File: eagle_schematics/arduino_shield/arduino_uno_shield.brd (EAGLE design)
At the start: 53 x 57.1 mm, 20 parts

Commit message: save
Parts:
- removed A1, A2, A3, A4, A5, A6, A7, A8: (no value), SparkFun-Connectors:1X03
- removed AUDIO_JACK: (no value), SparkFun-Connectors:AUDIO-JACK
- removed FRAME3: FRAME-LETTER, SparkFun-Aesthetics:CREATIVE_COMMONS
- removed MCP3208: MCP3208-CI/P, Microchip_By_element14_Batch_1:DIP254P762X432-16
- removed MCP4921: MCP4921-E/P, Microchip_By_element14_Batch_1:DIP254P762X432-8
- added ADC1_MIC: (no value), SparkFun-Connectors:1X03_LOCK
- added ADC2, ADC3, ADC4: TRIMPOT-PTH-KNOB, SparkFun-Electromechanical:3386U
- added JP1: (no value), SparkFun-Connectors:AUDIO-JACK
- added R4: (no value), SparkFun-Resistors:AXIAL-0.3
- added U$2: MCP3204-CI/P, Microchip_By_element14_Batch_1:DIP254P762X432-14
- added U1: ARDUINO_R3_SHIELD, SparkFun-Boards:UNO_R3_SHIELD
- C1: device SparkFun-Passives:CAP-PTH-SMALL -> SparkFun-Capacitors:CAP-PTH-5MM
- C2: device SparkFun-Passives:CPOL-RADIAL-10UF-25V -> SparkFun-Capacitors:CPOL-RADIAL-10UF-25V
- EXT_LED: value M023.5MM -> M02LOCK; device SparkFun-Connectors:SCREWTERMINAL-3.5MM-2 -> SparkFun-Connectors:1X02_LOCK
- R1: value 1.5K -> 330; device SparkFun-Passives:AXIAL-0.4 -> SparkFun-Resistors:AXIAL-0.3
- R2: value 1K -> 1.5k; device SparkFun-Passives:AXIAL-0.4 -> SparkFun-Resistors:AXIAL-0.3
- R3: value 330 -> 1k; device SparkFun-Passives:AXIAL-0.4 -> SparkFun-Resistors:AXIAL-0.3
- U$1: value ARDUINO_R3_SHIELD -> MCP4921-E/P; device SparkFun-Boards:UNO_R3_SHIELD -> Microchip_By_element14_Batch_1:DIP254P762X432-8
- moved R3 53.6 mm to (26.7, 16.5), turned to 0 degrees
- moved C2 25.9 mm to (44.5, 16.5), turned to 0 degrees
- moved EXT_LED 20.4 mm to (30.5, 3.81)
- moved R2 20.4 mm to (26.7, 19.1)
- moved U$1 19.9 mm to (17.8, 11.4)
- moved C1 19.4 mm to (36.8, 15.2), turned to 0 degrees
- moved R1 16.6 mm to (14.0, 53.3)
- moved LED 15.3 mm to (15.2, 47.0), turned to 0 degrees
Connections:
- removed net AUD: A1.2, MCP3208.1
- removed net N$10: LED.A, R3.P$1
- removed net N$11: MCP4921.5, U$1.D8
- removed net N$12: EXT_LED.1, R3.P$2, U$1.D6
- removed net N$14: A3.2, MCP3208.3
- removed net N$15: A4.2, MCP3208.4
- removed net N$16: A6.2, MCP3208.6
- removed net N$17: A7.2, MCP3208.7
- removed net N$18: A8.2, MCP3208.8
- removed net N$8: C1.1, C2.1, R1.P$2
- removed net N$9: AUDIO_JACK.RING, AUDIO_JACK.TIP, C2.2, R2.P$2
- removed net SPI_CLK: MCP3208.13, MCP4921.3, U$1.D13
- removed net SPI_MISO: MCP3208.12, U$1.D12
- removed net SPI_MOSI: MCP3208.11, MCP4921.4, U$1.D11
- new net ADC1: ADC1_MIC.1, U$2.1
- new net ADC2: ADC2.2, U$2.2
- new net ADC3: ADC3.2, U$2.3
- new net ADC4: ADC4.2, U$2.4
- new net LDAC: U$1.5, U1.D8
- new net LED: R1.P$1, R4.P$1, U1.D6
- new net MISO: U$2.10, U1.D12
- new net MOSI: U$1.4, U$2.9, U1.D11
- new net N$4: C2.2, JP1.RING, JP1.TIP, R3.P$2
- new net N$5: EXT_LED.1, R4.P$2
- new net SCK: U$1.3, U$2.11, U1.D13
- net 3.3V: now also ADC1_MIC.3, ADC2.1, ADC3.1, ADC4.1, U$1.6, U$2.13, U1.3.3V; no longer A1.3, A2.3, A3.3, A4.3, A5.3, A6.3, A7.3, A8.3, MCP3208.15, MCP4921.6, U$1.3.3V
- net 5V: now also U$1.1, U$2.14, U1.5V; no longer MCP3208.16, MCP4921.1, U$1.5V
- net CS_ADC: now also U$2.8, U1.D10; no longer MCP3208.10, U$1.D10
- net CS_DAC: now also U$1.2, U1.D9; no longer MCP4921.2, U$1.D9
- net GND: now also ADC1_MIC.2, ADC2.3, ADC3.3, ADC4.3, JP1.SLEEVE, R3.P$1, U$1.7, U$2.12, U$2.7, U1.GND@0; no longer A1.1, A2.1, A3.1, A4.1, A5.1, A6.1, A7.1, A8.1, AUDIO_JACK.SLEEVE, MCP3208.14, MCP3208.9, MCP4921.7, R2.P$1, U$1.GND@0, U$1.GND@1, U$1.GND@2
- net N$1: now also LED.A, R1.P$2; no longer A5.2, MCP3208.5
- net N$2: now also R2.P$1, U$1.8; no longer A2.2, MCP3208.2
- net N$3: now also C1.1, C2.1, R2.P$2; no longer MCP4921.8, R1.P$1
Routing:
- net GND: track 204.1 -> 0.00 mm
- net 3.3V: track 97.2 -> 0.00 mm
- net N$12: track 62.3 -> 0.00 mm
- net 5V: track 50.5 -> 0.00 mm
- net N$1: track 36.8 -> 0.00 mm
- net AUD: track 35.7 -> 0.00 mm
- net N$16: track 34.9 -> 0.00 mm
- net N$11: track 33.5 -> 0.00 mm
- net CS_DAC: track 33.3 -> 0.00 mm
- net N$2: track 32.1 -> 0.00 mm
- net SPI_MOSI: track 32.0 -> 0.00 mm
- net N$9: track 29.3 -> 0.00 mm
- net N$17: track 28.3 -> 0.00 mm
- net N$18: track 23.9 -> 0.00 mm
- net SPI_CLK: track 23.7 -> 0.00 mm
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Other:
- board text removed: "3V"
- board text removed: "GND"
- board text removed: "IN"
- board text removed: "Ultimate Voice Changer Shield v1.0.1"
- board text removed: "theotherandygrove.com"

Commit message: save
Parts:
- moved EXT_LED 20.5 mm to (48.3, 14.0)
- moved C2 14.5 mm to (33.0, 7.62), turned to 90 degrees
- moved C1 13.3 mm to (24.1, 11.4), turned to 180 degrees
- moved R3 10.5 mm to (24.1, 6.35)
- moved R4 10.2 mm to (40.6, 14.0)
- moved ADC2 3.81 mm to (39.4, 22.9)
- moved R2 3.59 mm to (24.1, 16.5)
- moved LED 3.59 mm to (12.7, 44.5), turned to 90 degrees
- moved R1 2.84 mm to (12.7, 50.8)
- moved U$1 2.84 mm to (16.5, 8.89)
- moved U$2 2.84 mm to (8.89, 36.8)
- moved ADC3 2.54 mm to (39.4, 35.6)
- moved ADC1_MIC 1.80 mm to (22.9, 31.8)
- moved ADC4 1.27 mm to (39.4, 48.3)
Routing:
- net GND: track 0.00 -> 164.3 mm
- net 3.3V: track 0.00 -> 97.3 mm
- net LED: track 0.00 -> 85.3 mm
- net 5V: track 0.00 -> 50.1 mm
- net LDAC: track 0.00 -> 46.3 mm
- net MOSI: track 0.00 -> 38.7 mm
- net ADC4: track 0.00 -> 33.3 mm
- net SCK: track 0.00 -> 31.1 mm
- net ADC3: track 0.00 -> 28.0 mm
- net N$4: track 0.00 -> 24.9 mm
- net ADC2: track 0.00 -> 23.4 mm
- net CS_DAC: track 0.00 -> 22.1 mm
- net MISO: track 0.00 -> 21.4 mm
- net ADC1: track 0.00 -> 12.9 mm
- net N$3: track 0.00 -> 12.8 mm
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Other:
- board text added: "3.3V"
- board text added: "ADC2"
- board text added: "ADC3"
- board text added: "ADC4"
- board text added: "AUD"
- board text added: "GND"
- board text added: "MCP3204"
- board text added: "MCP4921"
- board text added: "SuperAwesomeRobots.com"
- board text added: "Ultimate Voice Changer 1.1"

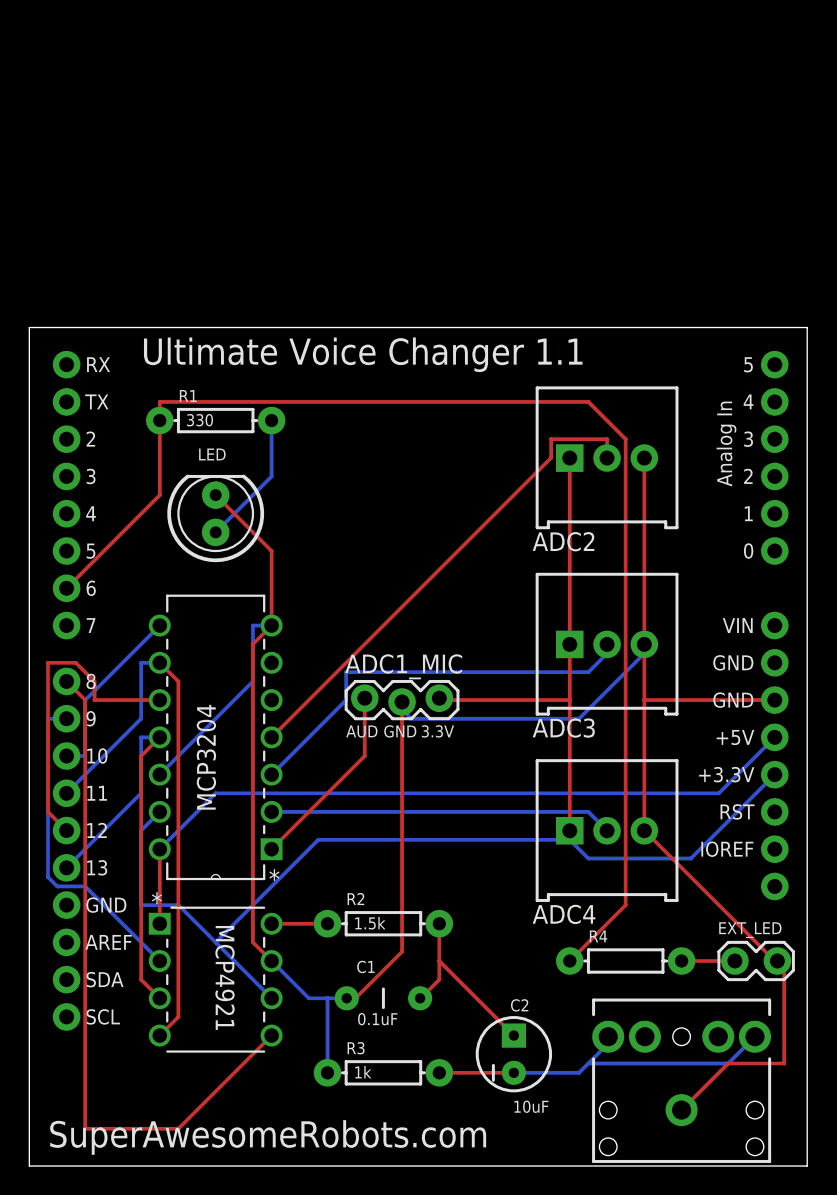
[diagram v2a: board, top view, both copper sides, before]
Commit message: small refinement to board layout
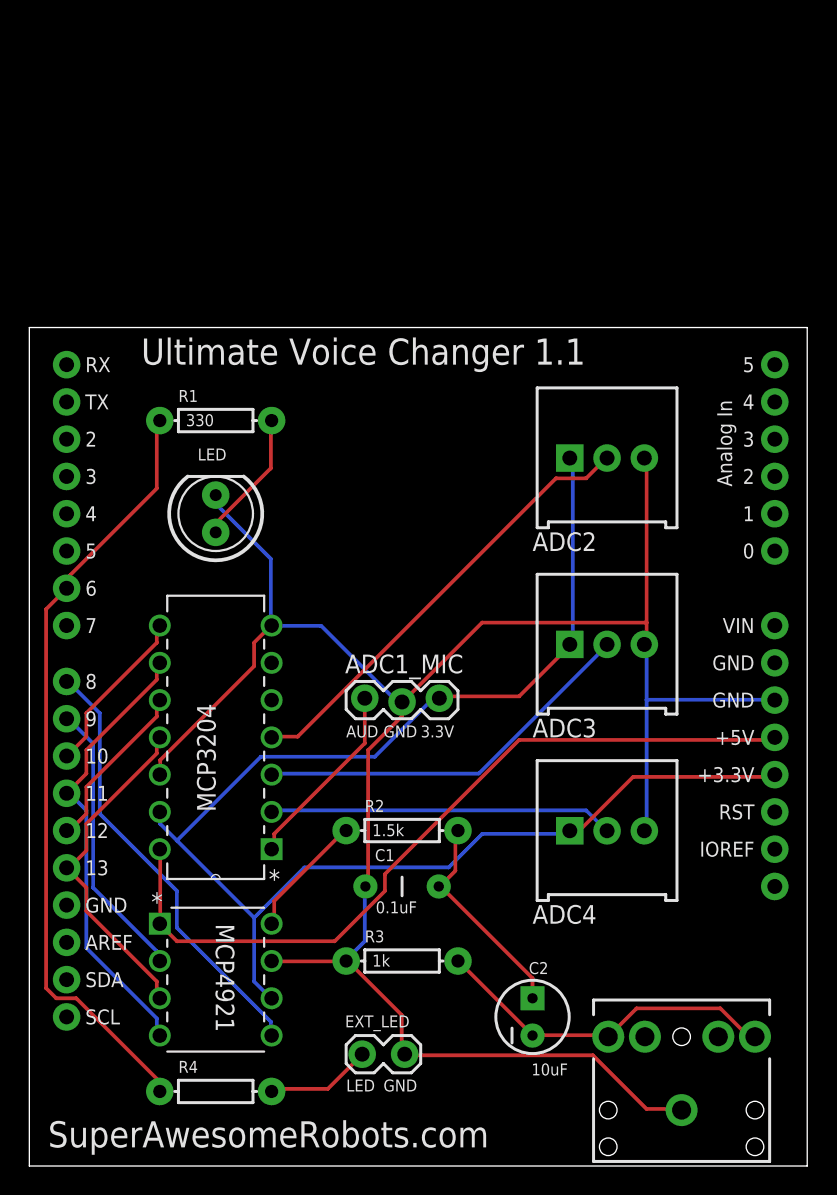
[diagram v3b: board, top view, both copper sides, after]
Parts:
- moved R4 29.3 mm to (12.7, 5.08)
- moved EXT_LED 26.2 mm to (22.9, 7.62)
- moved C1 7.73 mm to (25.4, 19.1)
- moved R3 7.73 mm to (25.4, 14.0)
- moved R2 6.48 mm to (25.4, 22.9)
- moved C2 2.84 mm to (34.3, 10.2)
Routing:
- net LED: track 85.3 -> 53.0 mm
- net GND: track 164.3 -> 141.2 mm
- net LDAC: track 46.3 -> 30.0 mm
- net MISO: track 21.4 -> 11.6 mm
- net SCK: track 31.1 -> 23.3 mm
- net MOSI: track 38.7 -> 31.0 mm
- net N$2: track 3.81 -> 8.51 mm
- net 5V: track 50.1 -> 54.0 mm
- net N$5: track 3.63 -> 7.23 mm
- net 3.3V: track 97.3 -> 100.9 mm
- net CS_DAC: track 22.1 -> 19.2 mm
- net ADC4: track 33.3 -> 30.7 mm
- net N$3: track 12.8 -> 14.8 mm
- net ADC3: track 28.0 -> 26.5 mm
- net N$4: track 24.9 -> 24.0 mm
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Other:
- board text added: "LED"

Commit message: change resistors from AXIAL-0.3 to AXIAL-0.4
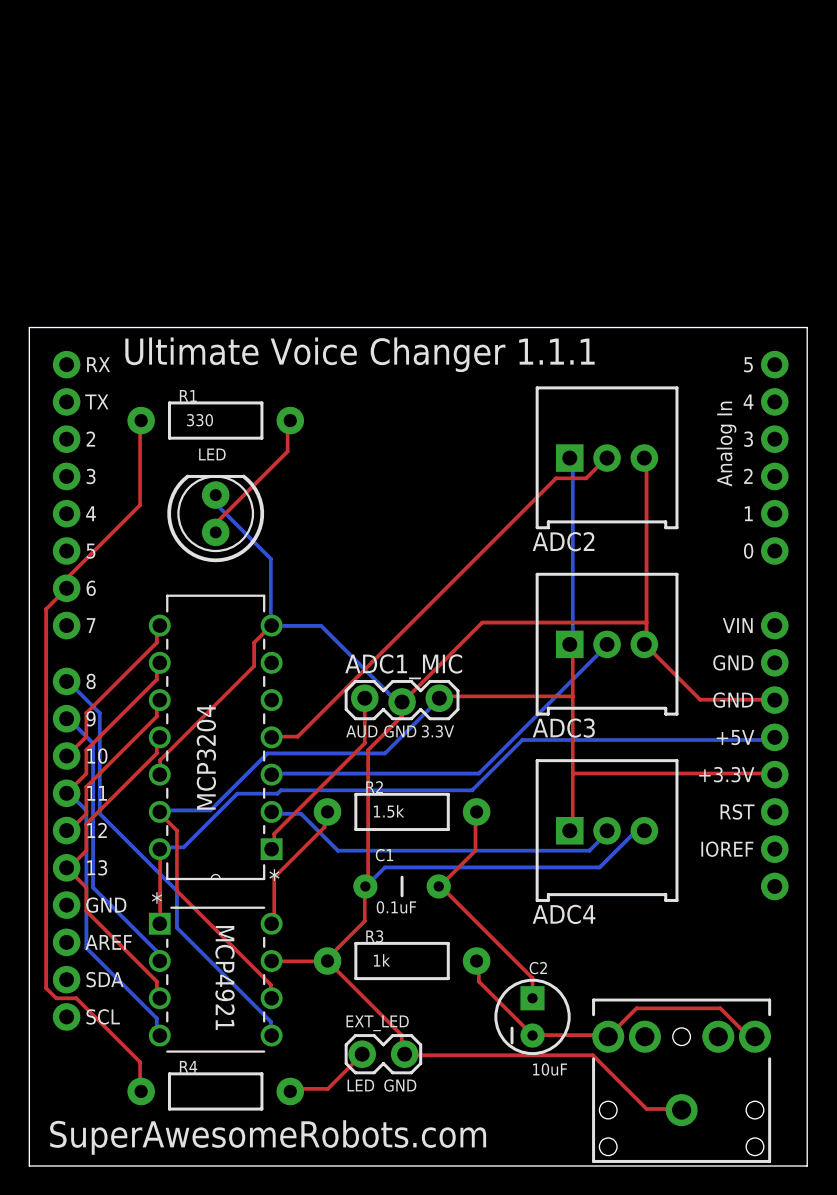
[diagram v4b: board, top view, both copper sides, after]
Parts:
- R1, R2, R3, R4: device SparkFun-Resistors:AXIAL-0.3 -> SparkFun-Resistors:AXIAL-0.4
- moved R2 1.27 mm to (25.4, 24.1)
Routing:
- net 3.3V: track 100.9 -> 87.2 mm
- net GND: track 141.2 -> 150.4 mm
- net 5V: track 54.0 -> 50.3 mm
- net N$3: track 14.8 -> 16.5 mm
- net N$5: track 7.23 -> 6.02 mm
- net LED: track 53.0 -> 51.9 mm
- net ADC2: track 23.5 -> 24.6 mm
- net N$2: track 8.51 -> 9.23 mm
- net N$1: track 9.24 -> 9.82 mm
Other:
- board text added: "Ultimate Voice Changer 1.1.1"
- board text removed: "Ultimate Voice Changer 1.1"
